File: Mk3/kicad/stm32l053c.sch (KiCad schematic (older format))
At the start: 14 parts, among them P1 SWD, U1 STM32L053C8_LQFP48, U2 ADS1015

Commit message: 3v3 LDO voltage regulator
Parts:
- removed W?: WIRE_ANT, Wire_Pads:SolderWirePad_single_2mmDrill, symbol TEST_1P
- added U?: AP2112, symbol AP2112
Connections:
- no-connect marks 2 -> 3
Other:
- note added: "3v3 Voltage Regulator"
- note added: "Antenna\n"
- note removed: "@TODO 3v3 voltage regulator"
- note removed: "ANTENNA Section\n"
- moved on the sheet: D1, P1, R4, U2, U?

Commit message: Basic pinout
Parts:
- removed C3: 20pF, Capacitors_SMD:C_0805_HandSoldering, symbol C
- gave numbers to parts that had none: 3
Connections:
- net labels added: +3.3V, I2C1_SCL, I2C1_SDA, SPI1_CS, SPI1_MISO, SPI1_MOSI, SPI1_SCK
- net labels removed: BOOT0, DIO0, DIO1, DIO2, DIO3, DIO4, DIO5, GND, MCO, OSC_OUT, PA1, PA10, PA11, PA12, PA15, PA2, PA3, PA4, PA5, PA6, PA7, PA8, PA9, PB0, PB1, PB10, PB11, PB12, PB13, PB14, PB15, PB2, PB4, PB5, PB6, PB7, PB8, PB9, PC13, RFM_VIN, SPI_SCK, SPI_SIMO, SPI_SOMI, SPI_nCS, nRESET
- wire segments 77 -> 44
- no-connect marks 3 -> 34
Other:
- note removed: "Absolute max of 3.6v"
- moved on the sheet: U5

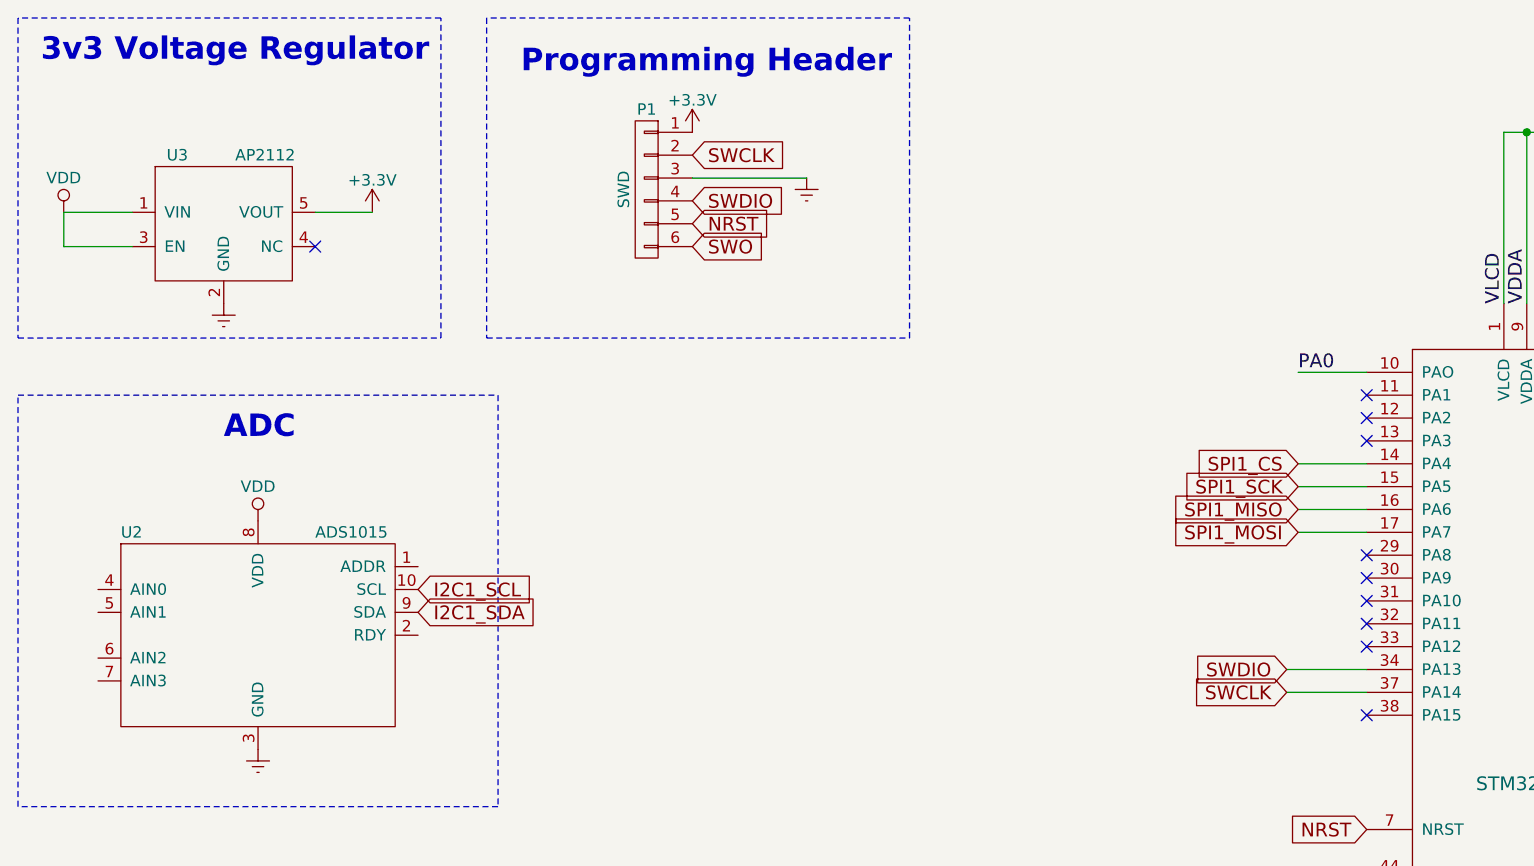
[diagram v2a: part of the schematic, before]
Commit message: More connections
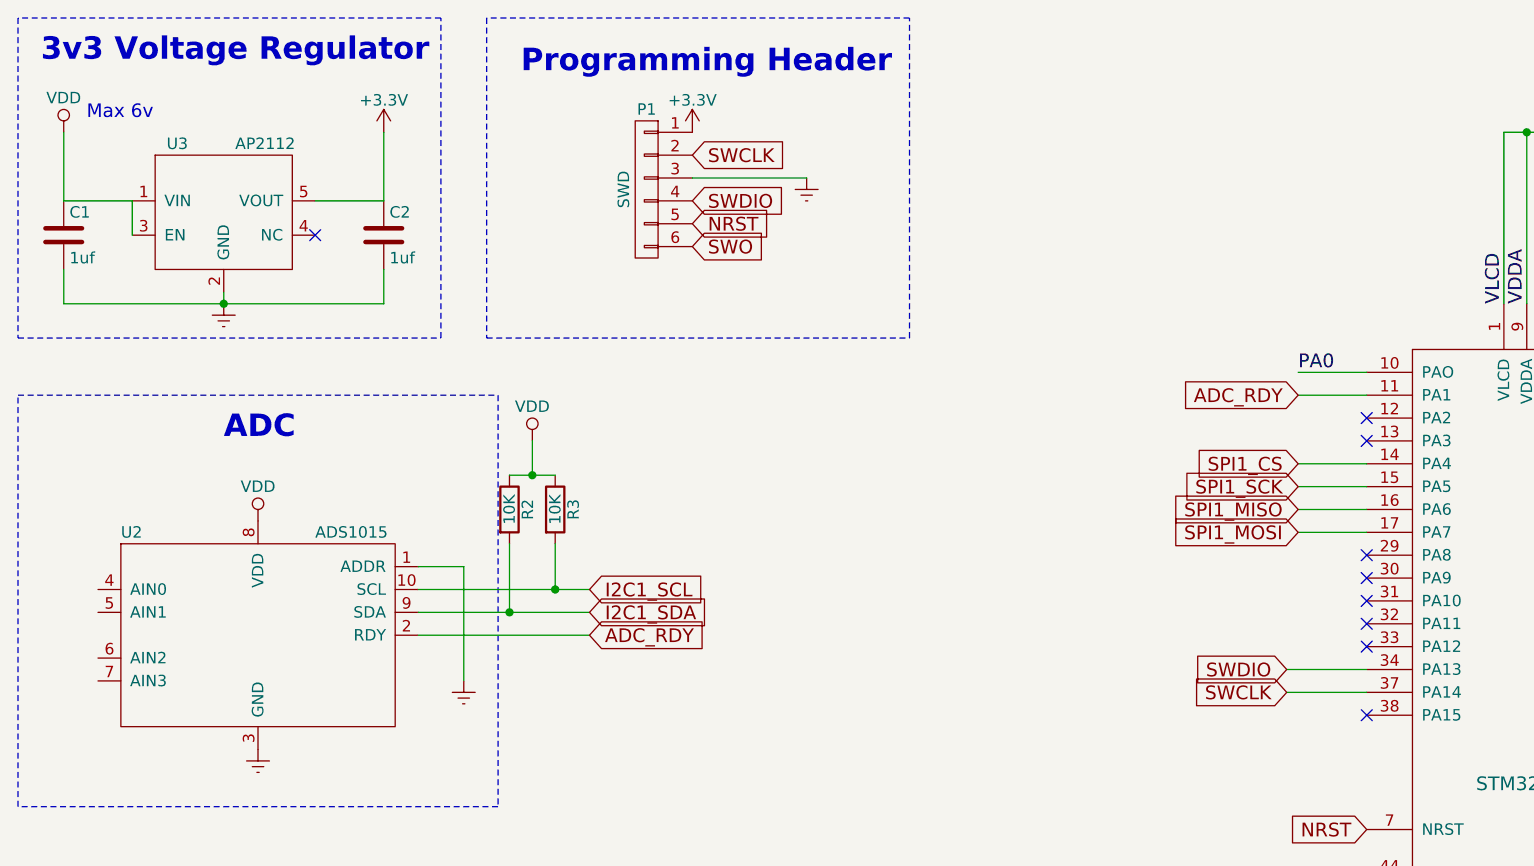
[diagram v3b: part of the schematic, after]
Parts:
- added C1, C2: 1uf, symbol C
- added R2, R3: 10K, symbol R
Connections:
- net +3V3: now also C1.1, C2.1, R2.1, R3.1
- net Earth: now also U2.1 (ADDR), C1.2, C2.2
- net I2C1_SCL: now also R3.2
- net I2C1_SDA: now also R2.2
- net ADC_RDY: now reaches U1.11 (PA1)
- net ADC_RDY: now also U2.2 (RDY)
- no-connect marks 34 -> 33
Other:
- note added: "Max 6v"
- moved on the sheet: U3
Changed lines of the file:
@@
 L AP2112 U3
 U 1 1 592F19AA
-P 1450 1400
-F 0 "U3" H 1200 1650 50  0000 L CNN
-F 1 "AP2112" H 1500 1650 50  0000 L CNN
-F 2 "" H 1400 1350 50  0001 C CNN
-F 3 "" H 550 1800 50  0001 C CNN
-	1    1450 1400
+P 1450 1350
+F 0 "U3" H 1200 1600 50  0000 L CNN
+F 1 "AP2112" H 1500 1600 50  0000 L CNN
+F 2 "" H 1400 1300 50  0001 C CNN
+F 3 "" H 550 1750 50  0001 C CNN
+	1    1450 1350
 	1    0    0    -1
 $EndComp
@@
 L VDD #PWR013
 U 1 1 592F1B4B
-P 750 1400
-F 0 "#PWR013" H 750 1250 50  0001 C CNN
-F 1 "VDD" H 750 1550 50  0000 C CNN
-F 2 "" H 750 1400 50  0000 C CNN
-F 3 "" H 750 1400 50  0000 C CNN
-	1    750  1400
-	1    0    0    -1
-$EndComp
-NoConn ~ 1850 1550
+P 750 1050
+F 0 "#PWR013" H 750 900 50  0001 C CNN
+F 1 "VDD" H 750 1200 50  0000 C CNN
+F 2 "" H 750 1050 50  0000 C CNN
+F 3 "" H 750 1050 50  0000 C CNN
+	1    750  1050
+	1    0    0    -1
+$EndComp
+NoConn ~ 1850 1500
 $Comp
 L Earth #PWR014
@@
 Text GLabel 8750 2700 2    60   Input ~ 0
 I2C1_SCL
-Text GLabel 2300 3050 2    60   Input ~ 0
+Text GLabel 3050 3050 2    60   Input ~ 0
 I2C1_SCL
-Text GLabel 2300 3150 2    60   Input ~ 0
+Text GLabel 3050 3150 2    60   Input ~ 0
 I2C1_SDA
 Text GLabel 6150 2800 0    60   Input ~ 0
@@
 L +3.3V #PWR015
 U 1 1 592F43A5
-P 2100 1400
-F 0 "#PWR015" H 2100 1250 50  0001 C CNN
-F 1 "+3.3V" H 2100 1540 50  0000 C CNN
-F 2 "" H 2100 1400 50  0001 C CNN
-F 3 "" H 2100 1400 50  0001 C CNN
-	1    2100 1400
-	1    0    0    -1
-$EndComp
-Wire Wire Line
-	1850 1400 2100 1400
-Wire Wire Line
-	750  1400 1050 1400
-Wire Wire Line
-	750  1400 750  1550
-Wire Wire Line
-	750  1550 1050 1550
+P 2150 1050
+F 0 "#PWR015" H 2150 900 50  0001 C CNN
+F 1 "+3.3V" H 2150 1190 50  0000 C CNN
+F 2 "" H 2150 1050 50  0001 C CNN
+F 3 "" H 2150 1050 50  0001 C CNN
+	1    2150 1050
+	1    0    0    -1
+$EndComp
 $Comp
 L +3.3V #PWR016
@@
 NoConn ~ 6450 4800
 NoConn ~ 6450 4900
-NoConn ~ 6450 2200
 NoConn ~ 6450 2300
 NoConn ~ 6450 2400
@@
 	1    0    0    -1
 $EndComp
+$Comp
+L R R3
+U 1 1 59300E59
+P 2900 2700
+F 0 "R3" V 2980 2700 50  0000 C CNN
+F 1 "10K" V 2900 2700 50  0000 C CNN
+F 2 "" V 2830 2700 50  0001 C CNN
+F 3 "" H 2900 2700 50  0001 C CNN
+	1    2900 2700
+	1    0    0    -1
+$EndComp
+$Comp
+L R R2
+U 1 1 59300F14
+P 2700 2700
+F 0 "R2" V 2780 2700 50  0000 C CNN
+F 1 "10K" V 2700 2700 50  0000 C CNN
+F 2 "" V 2630 2700 50  0001 C CNN
+F 3 "" H 2700 2700 50  0001 C CNN
+	1    2700 2700
+	1    0    0    -1
+$EndComp
+Wire Wire Line
+	2300 3050 3050 3050
+Wire Wire Line
+	3050 3150 2300 3150
+Wire Wire Line
+	2700 2850 2700 3150
+Connection ~ 2700 3150
+Wire Wire Line
+	2900 2850 2900 3050
+Connection ~ 2900 3050
+$Comp
+L VDD #PWR027
+U 1 1 593015DF
+P 2800 2400
+F 0 "#PWR027" H 2800 2250 50  0001 C CNN
+F 1 "VDD" H 2800 2550 50  0000 C CNN
+F 2 "" H 2800 2400 50  0000 C CNN
+F 3 "" H 2800 2400 50  0000 C CNN
+	1    2800 2400
+	1    0    0    -1
+$EndComp
+Wire Wire Line
+	2700 2550 2900 2550
+Wire Wire Line
+	2800 2400 2800 2550
+Connection ~ 2800 2550
+$Comp
+L Earth #PWR028
+U 1 1 59301904
+P 2500 3450
+F 0 "#PWR028" H 2500 3200 50  0001 C CNN
+F 1 "Earth" H 2500 3300 50  0001 C CNN
+F 2 "" H 2500 3450 50  0000 C CNN
+F 3 "" H 2500 3450 50  0000 C CNN
+	1    2500 3450
+	-1   0    0    -1
+$EndComp
+Wire Wire Line
+	2500 3450 2500 2950
+Wire Wire Line
+	2500 2950 2300 2950
+Text GLabel 3050 3250 2    60   Input ~ 0
+ADC_RDY
+Wire Wire Line
+	3050 3250 2300 3250
+Text GLabel 6150 2200 0    60   Input ~ 0
+ADC_RDY
+Wire Wire Line
+	6150 2200 6450 2200
+Text Notes 850  1000 0    59   ~ 0
+Max 6v
+$Comp
+L C C1
+U 1 1 59302470
+P 750 1500
+F 0 "C1" H 775 1600 50  0000 L CNN
+F 1 "1uf" H 775 1400 50  0000 L CNN
+F 2 "" H 788 1350 50  0001 C CNN
+F 3 "" H 750 1500 50  0001 C CNN
+	1    750  1500
+	1    0    0    -1
+$EndComp
+Wire Wire Line
+	1450 1750 1450 1800
+Wire Wire Line
+	750  1800 2150 1800
+Wire Wire Line
+	750  1800 750  1650
+Wire Wire Line
+	1850 1350 2150 1350
+Wire Wire Line
+	2150 1350 2150 1050
+Wire Wire Line
+	750  1350 750  1050
+$Comp
+L C C2
+U 1 1 5930294B
+P 2150 1500
+F 0 "C2" H 2175 1600 50  0000 L CNN
+F 1 "1uf" H 2175 1400 50  0000 L CNN
+F 2 "" H 2188 1350 50  0001 C CNN
+F 3 "" H 2150 1500 50  0001 C CNN
+	1    2150 1500
+	1    0    0    -1
+$EndComp
+Wire Wire Line
+	2150 1800 2150 1650
+Connection ~ 1450 1800
+Wire Wire Line
+	1050 1350 750  1350
+Wire Wire Line
+	1050 1500 1050 1350
 $EndSCHEMATC
